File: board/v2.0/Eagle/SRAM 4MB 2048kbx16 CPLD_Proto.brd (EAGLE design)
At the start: 58.2 x 49.6 mm, 26 parts, among them IC1 AS6C3216-55, IC2 74LCX245MTC, IC3 74LCX245MTC, IC4 74LCX245MTC, IC5 74LCX541TTR, IC6 74LCX541TTR, IC7 74LCX541TTR, IC8 XC9536_44VQ, IC9 TLV70033DDCT, SW1 RAM/Disk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

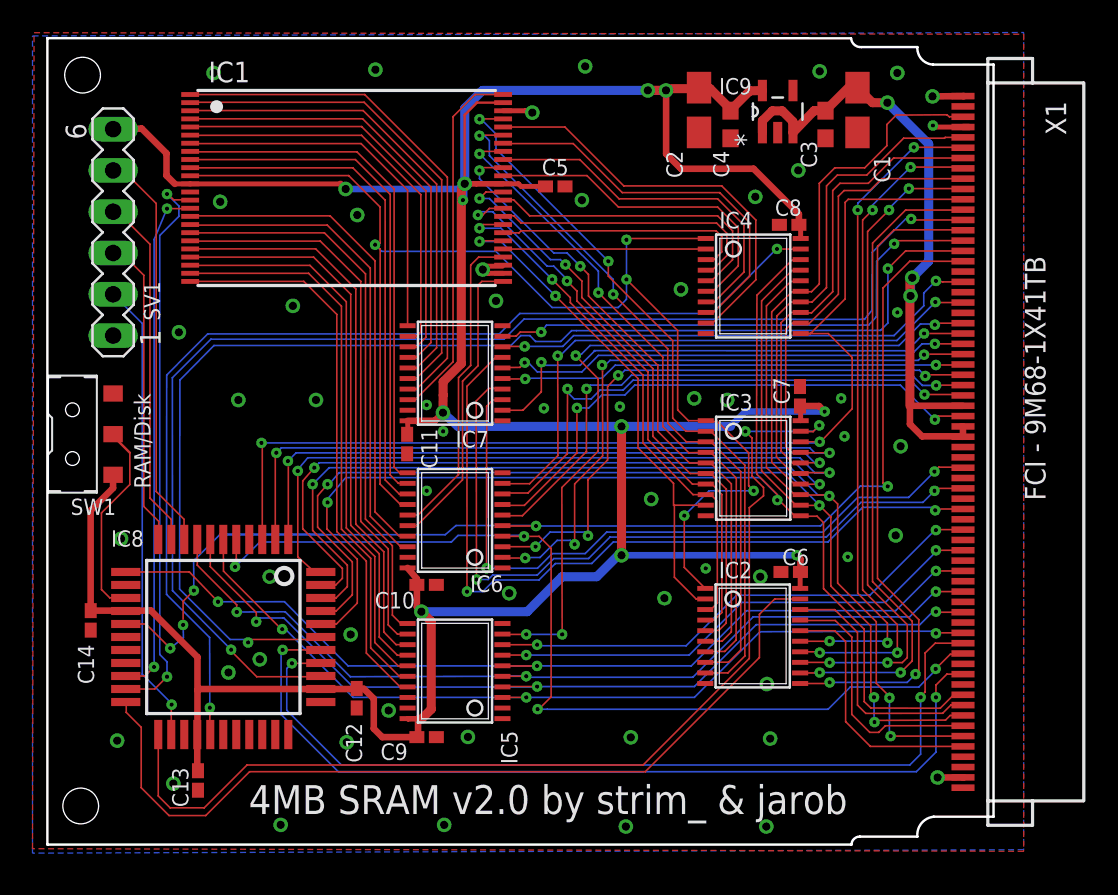
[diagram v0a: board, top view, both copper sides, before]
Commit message: Small change in the boards v2.0 and v2.1
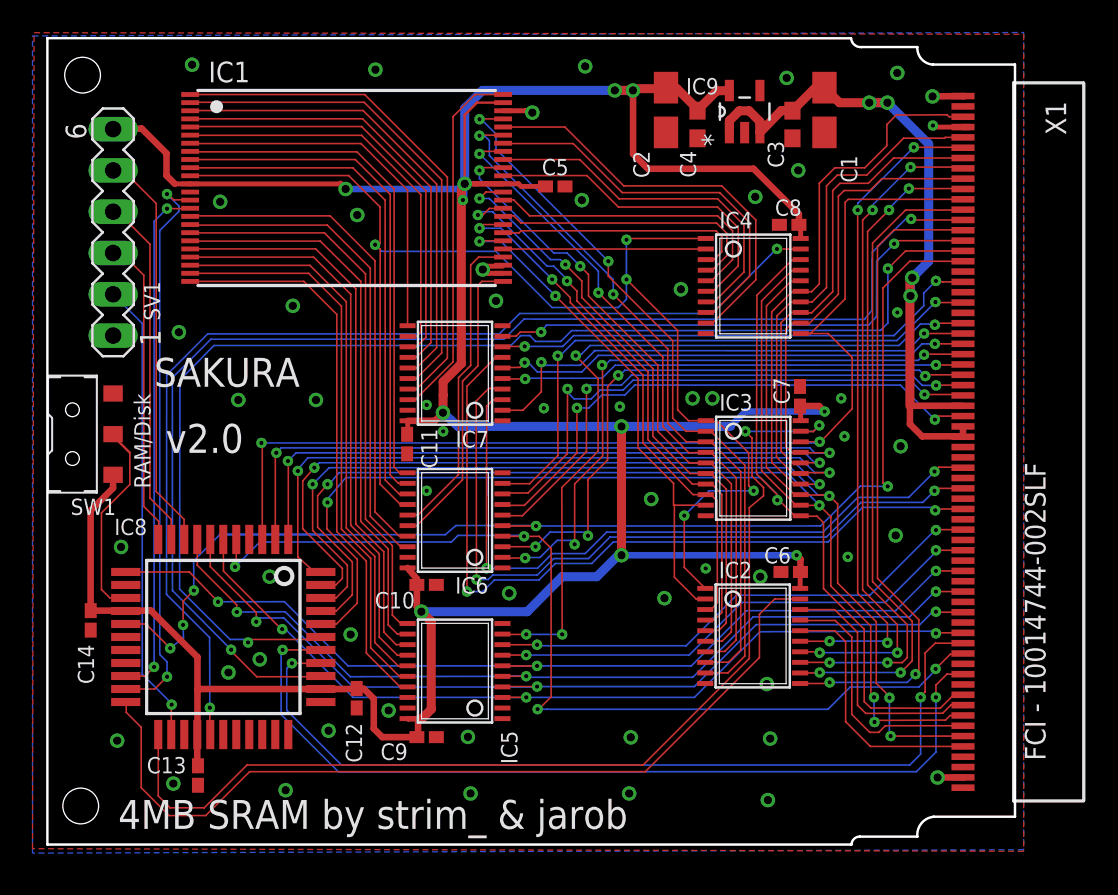
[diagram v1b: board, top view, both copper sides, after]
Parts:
- IC8: value XC9536_44VQ -> XC9536XL_44VQ
- moved C1 2.03 mm to (88.3, 62.1)
- moved C2 2.03 mm to (78.5, 62.1)
- moved C3 2.03 mm to (86.3, 61.2)
- moved C4 2.03 mm to (80.5, 61.2)
- moved IC9 2.03 mm to (83.4, 62.0)
- moved C13 0.30 mm to (49.7, 21.2)
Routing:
- net +5V: track 41.2 -> 44.4 mm, vias 3 -> 4
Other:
- board size 58.2 x 49.6 mm -> 59.5 x 49.6 mm
- board text added: "4MB SRAM by strim_ & jarob"
- board text added: "SAKURA"
- board text added: "v2.0"
- board text removed: "4MB SRAM v2.0 by strim_ & jarob"
